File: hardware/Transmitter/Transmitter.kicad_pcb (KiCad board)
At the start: 4 copper layers, 58.5 x 58.5 mm, 75 parts, among them IC1 ESP32-C3-MINI-1-N4, J1 USB_C_Receptacle_USB2.0, J2 UP_BTN, J3 DN_BTN, J4 Conn_01x03, J5 UART, Q1 2N7002, SW1 Reset, SW2 SW_SPST, U1 TPS22810DRV, U2 TPS22810DRV, U3 AZ1117-3.3

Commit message: Removed old files
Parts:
- added Q10: NChan, Package_TO_SOT_SMD:SOT-23, F.Cu at (144.3, 67.2)
- added Q11: NChan, Package_TO_SOT_SMD:SOT-23, F.Cu at (144.3, 59.0)
- added Q2: NChan, Package_TO_SOT_SMD:SOT-23, F.Cu at (141.3, 79.0)
- added Q3: NChan, Package_TO_SOT_SMD:SOT-23, F.Cu at (141.3, 71.0)
- added Q4: NChan, Package_TO_SOT_SMD:SOT-23, F.Cu at (141.3, 62.9)
- added Q5: PChan, Package_TO_SOT_SMD:SOT-23, F.Cu at (137.9, 79.0)
- added Q6: PChan, Package_TO_SOT_SMD:SOT-23, F.Cu at (137.8, 71.0)
- added Q7: PChan, Package_TO_SOT_SMD:SOT-23, F.Cu at (137.8, 62.9)
- added Q8: NChan, Package_TO_SOT_SMD:SOT-23, F.Cu at (144.3, 84.0)
- added Q9: NChan, Package_TO_SOT_SMD:SOT-23, F.Cu at (144.2, 75.1)
- added R21: 100k, Resistor_SMD:R_0402_1005Metric, F.Cu at (141.4, 81.5)
- added R22: 100k, Resistor_SMD:R_0402_1005Metric, F.Cu at (141.3, 73.4)
- added R23: 100k, Resistor_SMD:R_0402_1005Metric, F.Cu at (141.2, 65.4)
- added R24: 100k, Resistor_SMD:R_0402_1005Metric, F.Cu at (135.8, 79.3)
- added R25: 100k, Resistor_SMD:R_0402_1005Metric, F.Cu at (135.7, 70.8)
- added R26: 100k, Resistor_SMD:R_0402_1005Metric, F.Cu at (135.7, 62.8)
- added R27: 282k, Resistor_SMD:R_0402_1005Metric, F.Cu at (137.7, 81.5)
- added R28: 100k, Resistor_SMD:R_0402_1005Metric, F.Cu at (139.6, 81.5)
- added R29: 155k, Resistor_SMD:R_0402_1005Metric, F.Cu at (137.6, 73.4)
- added R30: 100k, Resistor_SMD:R_0402_1005Metric, F.Cu at (139.4, 73.4)
- added R31: 28k, Resistor_SMD:R_0402_1005Metric, F.Cu at (137.4, 65.4)
- added R32: 100k, Resistor_SMD:R_0402_1005Metric, F.Cu at (139.3, 65.4)
- added R33: 400, Resistor_SMD:R_2010_5025Metric, F.Cu at (139.4, 83.6)
- added R34: 400, Resistor_SMD:R_2010_5025Metric, F.Cu at (139.3, 75.5)
- added R35: 400, Resistor_SMD:R_2010_5025Metric, F.Cu at (139.3, 67.5)
- added R36: 400, Resistor_SMD:R_2010_5025Metric, F.Cu at (139.3, 59.3)
- moved J2 44.3 mm to (154.1, 112.2), turned to 90 degrees
- moved J3 36.9 mm to (148.1, 112.2), turned to 90 degrees
- renumbered C2 to C1, C11 to C10, C12 to C11, C13 to C12, C14 to C13, C15 to C14, C16 to C15, C17 to C16, C18 to C17, C19 to C18, C20 to C19, C3 to C2, C21 to C20, C22 to C21, C23 to C22, C24 to C23, C25 to C24, C26 to C25, C27 to C26, C28 to C27, C29 to C28, C30 to C29, C4 to C3, C31 to C30, C5 to C4, C6 to C5, C7 to C6, C8 to C7, C9 to C8, C10 to C9
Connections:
- IC1 pad 11: unconnected-(IC1-IO32-Pad11) -> /M3
- IC1 pad 12: unconnected-(IC1-IO33-Pad12) -> /S3
- IC1 pad 13: unconnected-(IC1-IO25-Pad13) -> /S2
- IC1 pad 15: unconnected-(IC1-IO27-Pad15) -> /C3
- IC1 pad 16: unconnected-(IC1-IO14-Pad16) -> /C1
- IC1 pad 31: unconnected-(IC1-IO23-Pad31) -> /M2
- IC1 pad 33: unconnected-(IC1-IO22-Pad33) -> /C2
- IC1 pad 5: unconnected-(IC1-I37-Pad5) -> /S4
- IC1 pad 6: unconnected-(IC1-I38-Pad6) -> /M4
- IC1 pad 7: unconnected-(IC1-I39-Pad7) -> /C4
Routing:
- net /UP_BTN: track 30.1 -> 3.18 mm
- net /DN_BTN: track 25.1 -> 2.83 mm

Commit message: Revision 1.2 of receiver board
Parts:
- removed Q10, Q11, Q2, Q3, Q4, Q8, Q9: NChan, Package_TO_SOT_SMD:SOT-23
- removed Q5, Q6, Q7: PChan, Package_TO_SOT_SMD:SOT-23
- removed R21, R22, R23, R24, R25, R26, R28, R30, R32: 100k, Resistor_SMD:R_0402_1005Metric
- removed R27: 282k, Resistor_SMD:R_0402_1005Metric
- removed R29: 155k, Resistor_SMD:R_0402_1005Metric
- removed R31: 28k, Resistor_SMD:R_0402_1005Metric
- removed R33, R34, R35, R36: 400, Resistor_SMD:R_2010_5025Metric
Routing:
- net Net-(J1-CC2): track 8.00 -> 9.99 mm
- net /VUSB: track 67.9 -> 66.0 mm, vias 3 -> 4
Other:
- board text added: "JLCJLCJLCJLC"

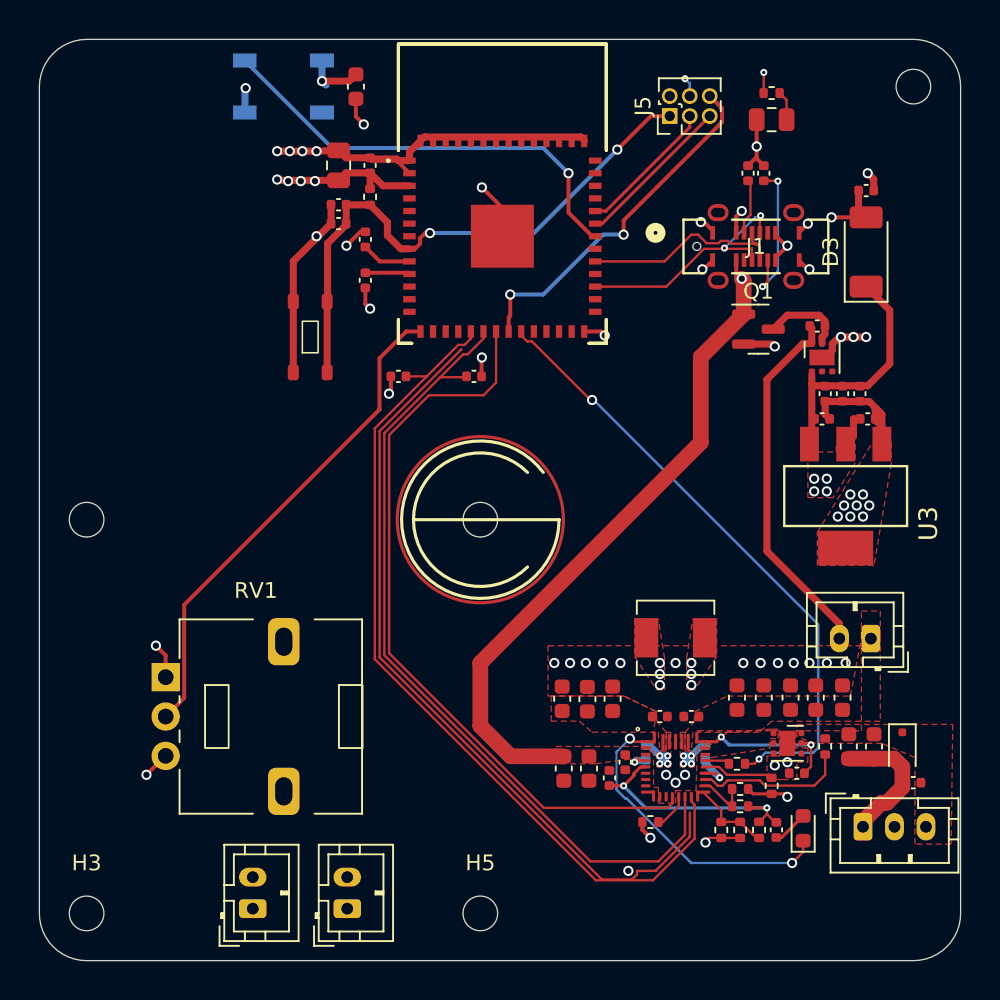
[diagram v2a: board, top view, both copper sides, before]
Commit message: BMS added to hardware
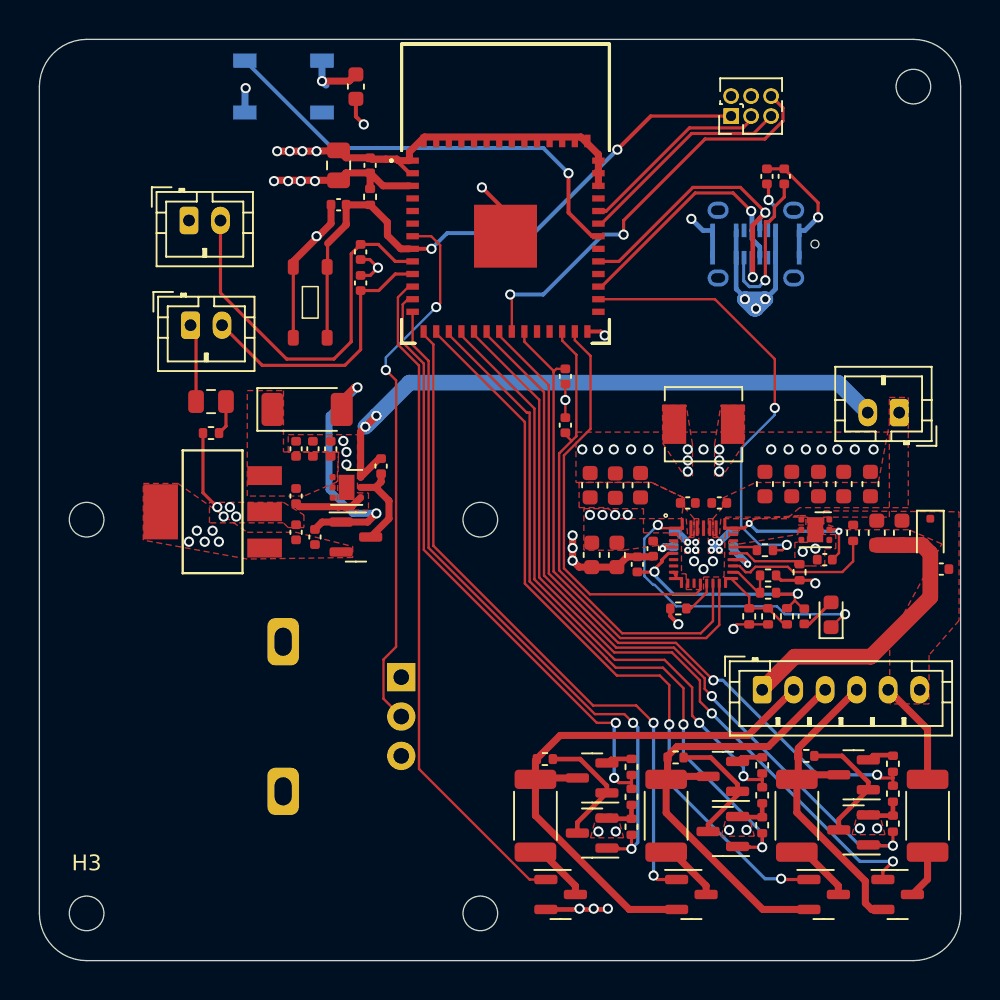
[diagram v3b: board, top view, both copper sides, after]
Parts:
- removed the C27 at (187.1, 81.1)
- removed the C3 at (153.5, 68.7)
- removed the J4 at (186.8, 107.0)
- removed the R14 at (155.2, 72.3)
- removed the R3 at (179.5, 65.5)
- added C25: 10u, Capacitor_SMD:C_0402_1005Metric, F.Cu at (150.8, 86.0)
- added J5: JST_PH, Connector_JST:JST_PH_B6B-PH-K_1x06_P2.00mm_Vertical, F.Cu at (180.4, 98.3)
- added Q10: NChan, Package_TO_SOT_SMD:SOT-23, F.Cu at (175.9, 111.3)
- added Q11: NChan, Package_TO_SOT_SMD:SOT-23, F.Cu at (167.6, 111.3)
- added Q2: NChan, Package_TO_SOT_SMD:SOT-23, F.Cu at (186.2, 107.2)
- added Q3: NChan, Package_TO_SOT_SMD:SOT-23, F.Cu at (177.9, 107.3)
- added Q4: NChan, Package_TO_SOT_SMD:SOT-23, F.Cu at (169.6, 107.4)
- added Q5: PChan, Package_TO_SOT_SMD:SOT-23, F.Cu at (186.2, 103.7)
- added Q6: PChan, Package_TO_SOT_SMD:SOT-23, F.Cu at (177.9, 103.8)
- added Q7: PChan, Package_TO_SOT_SMD:SOT-23, F.Cu at (169.6, 103.9)
- added Q8: NChan, Package_TO_SOT_SMD:SOT-23, F.Cu at (189.0, 111.3)
- added Q9: NChan, Package_TO_SOT_SMD:SOT-23, F.Cu at (184.3, 111.3)
- added R10: 100k, Capacitor_SMD:C_0402_1005Metric, F.Cu at (154.9, 72.5)
- added R21: 100k, Resistor_SMD:R_0402_1005Metric, F.Cu at (188.7, 106.8)
- added R22: 100k, Resistor_SMD:R_0402_1005Metric, F.Cu at (180.4, 106.9)
- added R23: 100k, Resistor_SMD:R_0402_1005Metric, F.Cu at (172.1, 107.0)
- added R24: 100k, Resistor_SMD:R_0402_1005Metric, F.Cu at (183.2, 102.5)
- added R25: 100k, Resistor_SMD:R_0402_1005Metric, F.Cu at (174.9, 102.6)
- added R26: 100k, Resistor_SMD:R_0402_1005Metric, F.Cu at (166.6, 102.7)
- added R27: 282k, Resistor_SMD:R_0402_1005Metric, F.Cu at (188.7, 103.0)
- added R28: 100k, Resistor_SMD:R_0402_1005Metric, F.Cu at (188.7, 104.9)
- added R29: 155k, Resistor_SMD:R_0402_1005Metric, F.Cu at (180.4, 103.1)
- added R30: 100k, Resistor_SMD:R_0402_1005Metric, F.Cu at (180.4, 105.0)
- added R31: 28k, Resistor_SMD:R_0402_1005Metric, F.Cu at (172.1, 103.2)
- added R32: 100k, Resistor_SMD:R_0402_1005Metric, F.Cu at (172.1, 105.1)
- added R33: 400, Resistor_SMD:R_2010_5025Metric, F.Cu at (190.9, 106.3)
- added R34: 400, Resistor_SMD:R_2010_5025Metric, F.Cu at (182.6, 106.3)
- added R35: 400, Resistor_SMD:R_2010_5025Metric, F.Cu at (174.3, 106.3)
- added R36: 400, Resistor_SMD:R_2010_5025Metric, F.Cu at (166.0, 106.3)
- added R5: 5.1k, Capacitor_SMD:C_0402_1005Metric, F.Cu at (181.8, 65.7)
- C26: value 10u -> 22u
- J1, RV1: moved to B.Cu
- moved J2 44.8 mm to (144.0, 68.5), turned to 0 degrees
- moved R6 41.6 mm to (145.4, 82.0)
- moved U3 40.2 mm to (145.5, 87.0), turned to 180 degrees
- moved D2 39.8 mm to (145.4, 80.0)
- moved J3 37.3 mm to (144.1, 75.2), turned to 0 degrees
- moved D3 36.9 mm to (151.5, 80.5), turned to 0 degrees
- moved C16 36.0 mm to (150.8, 83.0), turned to 90 degrees
- moved R8 34.6 mm to (152.0, 88.6), turned to -90 degrees
- moved C26 34.2 mm to (150.8, 88.3), turned to -90 degrees
- moved C20 33.8 mm to (151.9, 83.0), turned to 90 degrees
- moved R7 32.3 mm to (154.9, 70.5), turned to -90 degrees
- moved C23 31.6 mm to (153.0, 83.0), turned to 90 degrees
- moved U1 31.3 mm to (154.0, 85.5), turned to 0 degrees
- moved Q1 28.8 mm to (154.6, 88.6)
- moved SW2 14.5 mm to (189.1, 80.7)
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- renumbered C11 to C10, C12 to C11, C13 to C12, C14 to C13, C15 to C14, C25 to C15, C28 to C27, C29 to C28, C30 to C29, C4 to C3, C5 to C4, C6 to C5, C7 to C6, C8 to C7, C9 to C8, C10 to C9, J5 to J4, R10 to R11, R11 to R12, R12 to R13, R13 to R14, R5 to R3
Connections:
- C26 pad 1: /VBUS -> +3.3V
- IC1 pad 11: /M3 -> /C4
- IC1 pad 12: /S3 -> /S4
- IC1 pad 13: /S2 -> /M4
- IC1 pad 14: /POT -> /C3
- IC1 pad 15: /C3 -> /C2
- IC1 pad 16: /C1 -> /M3
- IC1 pad 17: unconnected-(IC1-IO12-Pad17) -> /S3
- IC1 pad 18: /SDA -> /C1
- IC1 pad 19: /SCL -> /M2
- IC1 pad 20: /QON -> /S2
- IC1 pad 22: /BC_INT -> /SDA
- IC1 pad 25: unconnected-(IC1-IO9-Pad25) -> /SCL
- IC1 pad 26: unconnected-(IC1-IO10-Pad26) -> /QON
- IC1 pad 29: unconnected-(IC1-IO5-Pad29) -> /BC_INT
- IC1 pad 31: /M2 -> unconnected-(IC1-IO23-Pad31)
- IC1 pad 33: /C2 -> unconnected-(IC1-IO22-Pad33)
- IC1 pad 5: /S4 -> unconnected-(IC1-I37-Pad5)
- IC1 pad 6: /M4 -> unconnected-(IC1-I38-Pad6)
- IC1 pad 7: /C4 -> /POT
- R4 pad 1: Net-(J1-CC2) -> Net-(J1-CC1)
- R7 pad 1: /VUSB -> /UP_BTN
- R7 pad 2: GND -> +3.3V
- R8 pad 1: Net-(Q1-D) -> /VUSB
- R8 pad 2: Net-(SW2-B) -> GND
- R9 pad 1: /UP_BTN -> Net-(Q1-D)
- R9 pad 2: +3.3V -> Net-(SW2-B)
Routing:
- net /SDA: track 105.0 -> 32.1 mm
- net /C1: track 0.00 -> 49.5 mm, vias 0 -> 2
- net /M2: track 0.00 -> 49.2 mm, vias 0 -> 2
- net /C2: track 0.00 -> 47.8 mm, vias 0 -> 2
- net /M3: track 0.00 -> 45.3 mm, vias 0 -> 2
- net /S2: track 0.00 -> 44.8 mm, vias 0 -> 2
- net /C3: track 0.00 -> 43.8 mm, vias 0 -> 2
- net /M4: track 0.00 -> 43.8 mm, vias 0 -> 2
- net /C4: track 0.00 -> 42.7 mm
- net /S3: track 0.00 -> 39.7 mm, vias 0 -> 2
- net /S4: track 0.00 -> 39.3 mm, vias 0 -> 2
- net /BAT_C: track 0.00 -> 36.1 mm
- net /BAT_B: track 0.00 -> 29.7 mm
- net GND: track 86.9 -> 112.1 mm, vias 51 -> 52
- net /UP_BTN: track 3.18 -> 25.3 mm
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- added copper zone on F.Cu, net /VBUS

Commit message: add battery balancing to transmitter
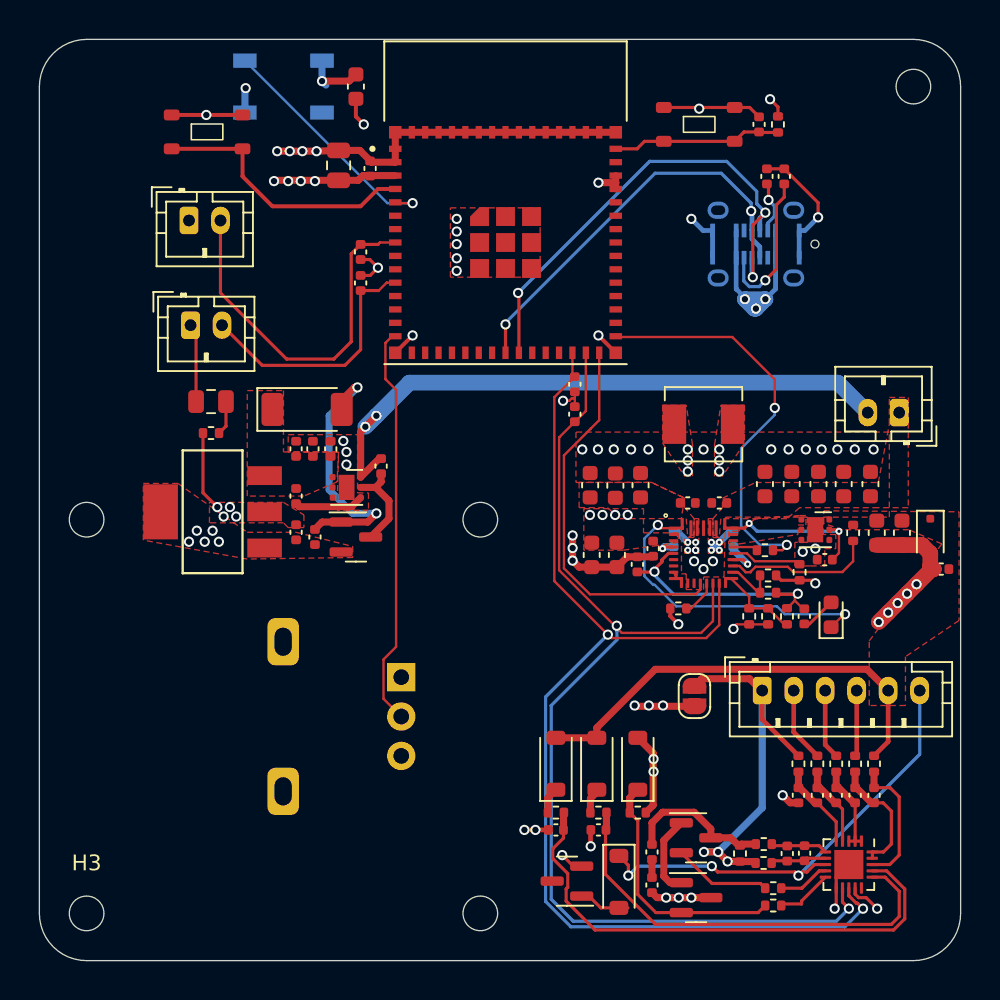
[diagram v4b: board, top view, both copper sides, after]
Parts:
- removed IC1: ESP32-C3-MINI-1-N4, ESP32MINI1N4:ESP32MINI1N4
- removed J4: UART, Connector_PinHeader_1.27mm:PinHeader_2x03_P1.27mm_Vertical
- removed J5: JST_PH, Connector_JST:JST_PH_B6B-PH-K_1x06_P2.00mm_Vertical
- removed Q10, Q11, Q2, Q3, Q4, Q8, Q9: NChan, Package_TO_SOT_SMD:SOT-23
- removed Q5, Q6, Q7: PChan, Package_TO_SOT_SMD:SOT-23
- removed R21, R22, R23, R24, R25, R26, R28, R30, R32: 100k, Resistor_SMD:R_0402_1005Metric
- removed R27: 282k, Resistor_SMD:R_0402_1005Metric
- removed R29: 155k, Resistor_SMD:R_0402_1005Metric
- removed R31: 28k, Resistor_SMD:R_0402_1005Metric
- removed R33, R34, R35, R36: 400, Resistor_SMD:R_2010_5025Metric
- added C30: 220nf, Capacitor_SMD:C_0402_1005Metric, F.Cu at (187.5, 105.0)
- added C31: 220nf, Capacitor_SMD:C_0402_1005Metric, F.Cu at (186.3, 105.0)
- added C32: 220nf, Capacitor_SMD:C_0402_1005Metric, F.Cu at (185.1, 105.0)
- added C33: 220nf, Capacitor_SMD:C_0402_1005Metric, F.Cu at (183.9, 105.0)
- added C34: 220nf, Capacitor_SMD:C_0402_1005Metric, F.Cu at (182.7, 105.0)
- added C35: 100p, Capacitor_SMD:C_0402_1005Metric, F.Cu at (182.0, 108.7)
- added C36: 0.1u, Capacitor_SMD:C_0402_1005Metric, F.Cu at (183.1, 108.7)
- added C37: 1u, Capacitor_SMD:C_0402_1005Metric, F.Cu at (167.3, 107.2)
- added C38: 1u, Capacitor_SMD:C_0402_1005Metric, F.Cu at (170.0, 107.2)
- added C39: 0.1u, Capacitor_SMD:C_0402_1005Metric, F.Cu at (173.4, 108.6)
- added C40: 0.1u, Capacitor_SMD:C_0402_1005Metric, F.Cu at (173.4, 110.7)
- added D6: 1N4148WQ-13-F, Diode_SMD:D_SOD-123, F.Cu at (167.3, 103.0)
- added D7: 1N4148WQ-13-F, Diode_SMD:D_SOD-123, F.Cu at (169.9, 103.0)
- added D8: 1N4148WQ-13-F, Diode_SMD:D_SOD-123, F.Cu at (171.3, 110.5)
- added D9: 1N4148WQ-13-F, Diode_SMD:D_SOD-123, F.Cu at (172.5, 103.0)
- added J6: JST_PH, Connector_JST:JST_PH_B6B-PH-K_1x06_P2.00mm_Vertical, F.Cu at (180.4, 98.3)
- added JP1: BQ76905_Bypass, Jumper:SolderJumper-2_P1.3mm_Open_RoundedPad1.0x1.5mm, F.Cu at (176.1, 98.7)
- added Q12: NMOS, Package_TO_SOT_SMD:SOT-23, F.Cu at (176.2, 107.7)
- added Q13: NMOS, Package_TO_SOT_SMD:SOT-23, F.Cu at (176.2, 111.5)
- added Q14: PMOS, Package_TO_SOT_SMD:SOT-23, F.Cu at (168.0, 110.5)
- added R37: 10, Resistor_SMD:R_0402_1005Metric, F.Cu at (187.5, 103.0)
- added R38: 10, Resistor_SMD:R_0402_1005Metric, F.Cu at (186.3, 103.0)
- added R39: 10, Resistor_SMD:R_0402_1005Metric, F.Cu at (185.1, 103.0)
- added R40: 10, Resistor_SMD:R_0402_1005Metric, F.Cu at (183.9, 103.0)
- added R41: 10, Resistor_SMD:R_0402_1005Metric, F.Cu at (182.7, 103.0)
- added R42: 100, Resistor_SMD:R_0402_1005Metric, F.Cu at (180.5, 109.3)
- added R43: 1m, Resistor_SMD:R_0402_1005Metric, F.Cu at (179.0, 108.7)
- added R44: 100, Resistor_SMD:R_0402_1005Metric, F.Cu at (167.3, 106.1)
- added R45: 100, Resistor_SMD:R_0402_1005Metric, F.Cu at (180.5, 108.1)
- added R46: 0, Resistor_SMD:R_0402_1005Metric, F.Cu at (170.0, 106.1)
- added R47: 5.1k, Resistor_SMD:R_0402_1005Metric, F.Cu at (181.1, 110.9)
- added R48: 5.1k, Resistor_SMD:R_0402_1005Metric, F.Cu at (181.1, 112.0)
- added R49: 100k, Resistor_SMD:R_0402_1005Metric, F.Cu at (172.5, 106.1)
- added SW3: Boot, Switch:Tactile_5.5mmx2.85mm, F.Cu at (145.2, 62.9)
- added U4: ESP32-S3-MINI-1-N8, XCVR_ESP32-S3-MINI-1-N8:XCVR_ESP32-S3-MINI-1-N8, F.Cu at (164.1, 69.9)
- added U5: ~, Package_DFN_QFN:UQFN-20-1EP_3x3mm_P0.4mm_EP1.85x1.85mm, F.Cu at (185.9, 109.4)
- moved C29 27.2 mm to (180.2, 62.4), turned to 90 degrees
- moved SW1 27.2 mm to (176.4, 62.4), turned to 0 degrees
- moved R20 26.3 mm to (181.4, 62.4)
- moved R19 0.92 mm to (168.5, 80.8)
- moved R18 0.78 mm to (168.5, 78.9)
- moved C28 0.20 mm to (155.5, 65.2)
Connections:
- net /TS renamed Net-(BQ25792RQMR1-TS)
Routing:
- net /C1: track 49.5 -> 0.00 mm, vias 2 -> 0
- net /M2: track 49.2 -> 0.00 mm, vias 2 -> 0
- net /C2: track 47.8 -> 0.00 mm, vias 2 -> 0
- net /M3: track 45.3 -> 0.00 mm, vias 2 -> 0
- net /S2: track 44.8 -> 0.00 mm, vias 2 -> 0
- net /C3: track 43.8 -> 0.00 mm, vias 2 -> 0
- net /M4: track 43.8 -> 0.00 mm, vias 2 -> 0
- net /C4: track 42.7 -> 0.00 mm
- net /S3: track 39.7 -> 0.00 mm, vias 2 -> 0
- net /SDA: track 32.1 -> 71.7 mm, vias 0 -> 2
- net /S4: track 39.3 -> 0.00 mm, vias 2 -> 0
- net /SCL: track 30.8 -> 69.0 mm, vias 0 -> 2
- net /BAT_C: track 36.1 -> 0.00 mm
- net Net-(U5-BAT): track 0.00 -> 33.3 mm
- net /BAT_B: track 29.7 -> 0.00 mm
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
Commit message: update emc
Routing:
- net /UP_BTN: track 23.8 -> 11.8 mm
- net /DN_BTN: track 16.4 -> 12.1 mm
- net /SDA: track 71.7 -> 73.8 mm
- net /POT: track 25.6 -> 26.7 mm
- net GND: track 107.4 -> 108.0 mm, vias 68 -> 187
- added copper zone on B.Cu, net GND

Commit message: create bom
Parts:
- H1, H2, H3, H4, H5: footprint MountingHole:MountingHole_2.2mm_M2 -> MountingHole:MountingHole_3.2mm_M3_DIN965_Pad_TopBottom
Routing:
- net /POT: track 26.7 -> 27.9 mm
- net /ESP_EN: track 10.8 -> 11.3 mm
- net GND: vias 187 -> 218

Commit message: PCB revision
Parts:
- removed C19, C22: 10u, Capacitor_SMD:C_0603_1608Metric
- added D10: TVN3V3B1S, Diode_SMD:D_0402_1005Metric, F.Cu at (150.8, 68.1)
- added D11: TVN3V3B1S, Diode_SMD:D_0402_1005Metric, F.Cu at (172.9, 65.1)
- added D12: TVN3V3B1S, Diode_SMD:D_0402_1005Metric, F.Cu at (179.6, 65.7)
- added D13: TVN3V3B1S, Diode_SMD:D_0402_1005Metric, F.Cu at (178.5, 65.7)
- added D14: TVN3V3B1S, Diode_SMD:D_0402_1005Metric, F.Cu at (187.1, 76.2)
- added R22: 10k, Resistor_SMD:R_0402_1005Metric, F.Cu at (163.3, 79.5)
- C11, C12, C13, C14, C15, C17, C18, C2, C5, C7, C9: footprint Capacitor_SMD:C_0603_1608Metric -> Capacitor_SMD:C_0805_2012Metric
- C16: footprint Capacitor_SMD:C_0402_1005Metric -> Capacitor_SMD:C_0805_2012Metric
- D3: value D_Schottky -> EVVOSS16
- D6, D7, D8, D9: footprint Diode_SMD:D_SOD-123 -> Diode_SMD:D_SOD-323
- L1: footprint Inductor_SMD:L_Sunlord_MWSA0402S -> Inductor_SMD:L_1008_2520Metric
- RV1: footprint Potentiometer_THT:Potentiometer_Alps_RK09L_Single_Vertical -> Potentiometer:Potentiometer_Bourns_PVT111-3
- moved D4 4.32 mm to (189.9, 92.7), turned to 180 degrees
- moved C17 2.58 mm to (181.4, 85.1)
- moved C13 2.08 mm to (183.5, 85.1)
- moved C12 1.68 mm to (185.6, 85.1)
- moved C24 1.26 mm to (190.6, 91.1)
- moved C11 1.04 mm to (173.7, 85.2)
- moved Q1 0.90 mm to (154.6, 89.5)
- moved U3 0.90 mm to (145.5, 87.9)
- moved D3 0.81 mm to (151.9, 79.8)
- moved C26 0.80 mm to (150.8, 89.1)
- moved C2 0.77 mm to (168.8, 89.7)
- moved C14 0.72 mm to (189.9, 88.7)
- moved C9 0.60 mm to (171.7, 85.2)
- moved R8 0.50 mm to (152.0, 89.1)
- moved C18 0.38 mm to (187.8, 88.7)
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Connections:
- U4 pad 22: /S3 -> Net-(U4-IO18/DAC2)
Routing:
- net /POT: track 27.9 -> 39.5 mm
- net GND: track 108.0 -> 100.2 mm, vias 218 -> 215
- net Net-(D14-A1): track 39.9 -> 44.0 mm
- net /VUSB: track 67.0 -> 69.8 mm
- net /D+: track 31.8 -> 34.0 mm
- net Net-(U4-IO18/DAC2): track 0.00 -> 2.10 mm
- net /D-: track 25.9 -> 27.4 mm
- net /QON: track 24.7 -> 26.0 mm
- net +3.3V: track 24.9 -> 26.0 mm, vias 13 -> 14
- net Net-(Q1-D): track 5.95 -> 6.85 mm
- net /SCL: track 68.9 -> 69.8 mm
- net Net-(D8-A): track 2.79 -> 1.96 mm
- net /ESP_IO0: track 17.3 -> 18.0 mm
- net Net-(D7-K): track 1.62 -> 2.25 mm
- net /BAT+: track 28.3 -> 28.9 mm
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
